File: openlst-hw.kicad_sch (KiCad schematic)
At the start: 54 parts, among them J1 CC Prog/Debug, J2 UART0, J7 Control Outputs, U1 CC1110, U2 MIC803, X1 TG2520SMN 27MHz

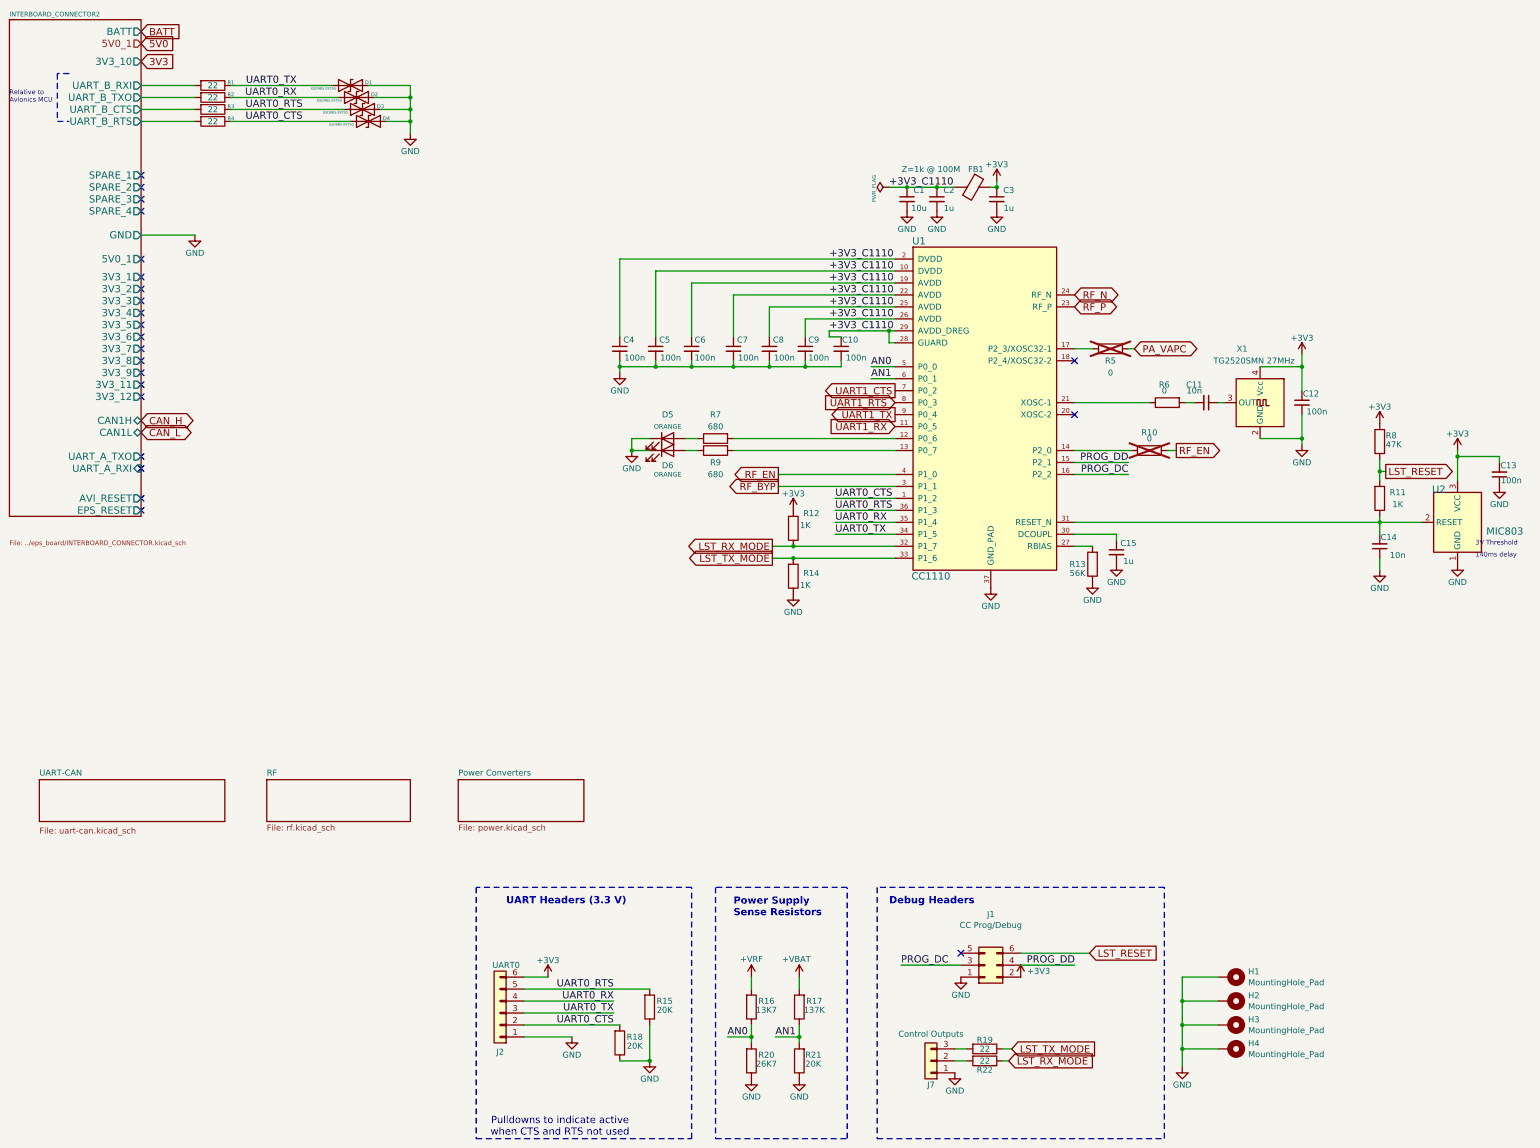
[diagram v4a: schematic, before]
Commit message: further refactor schema into subsheets
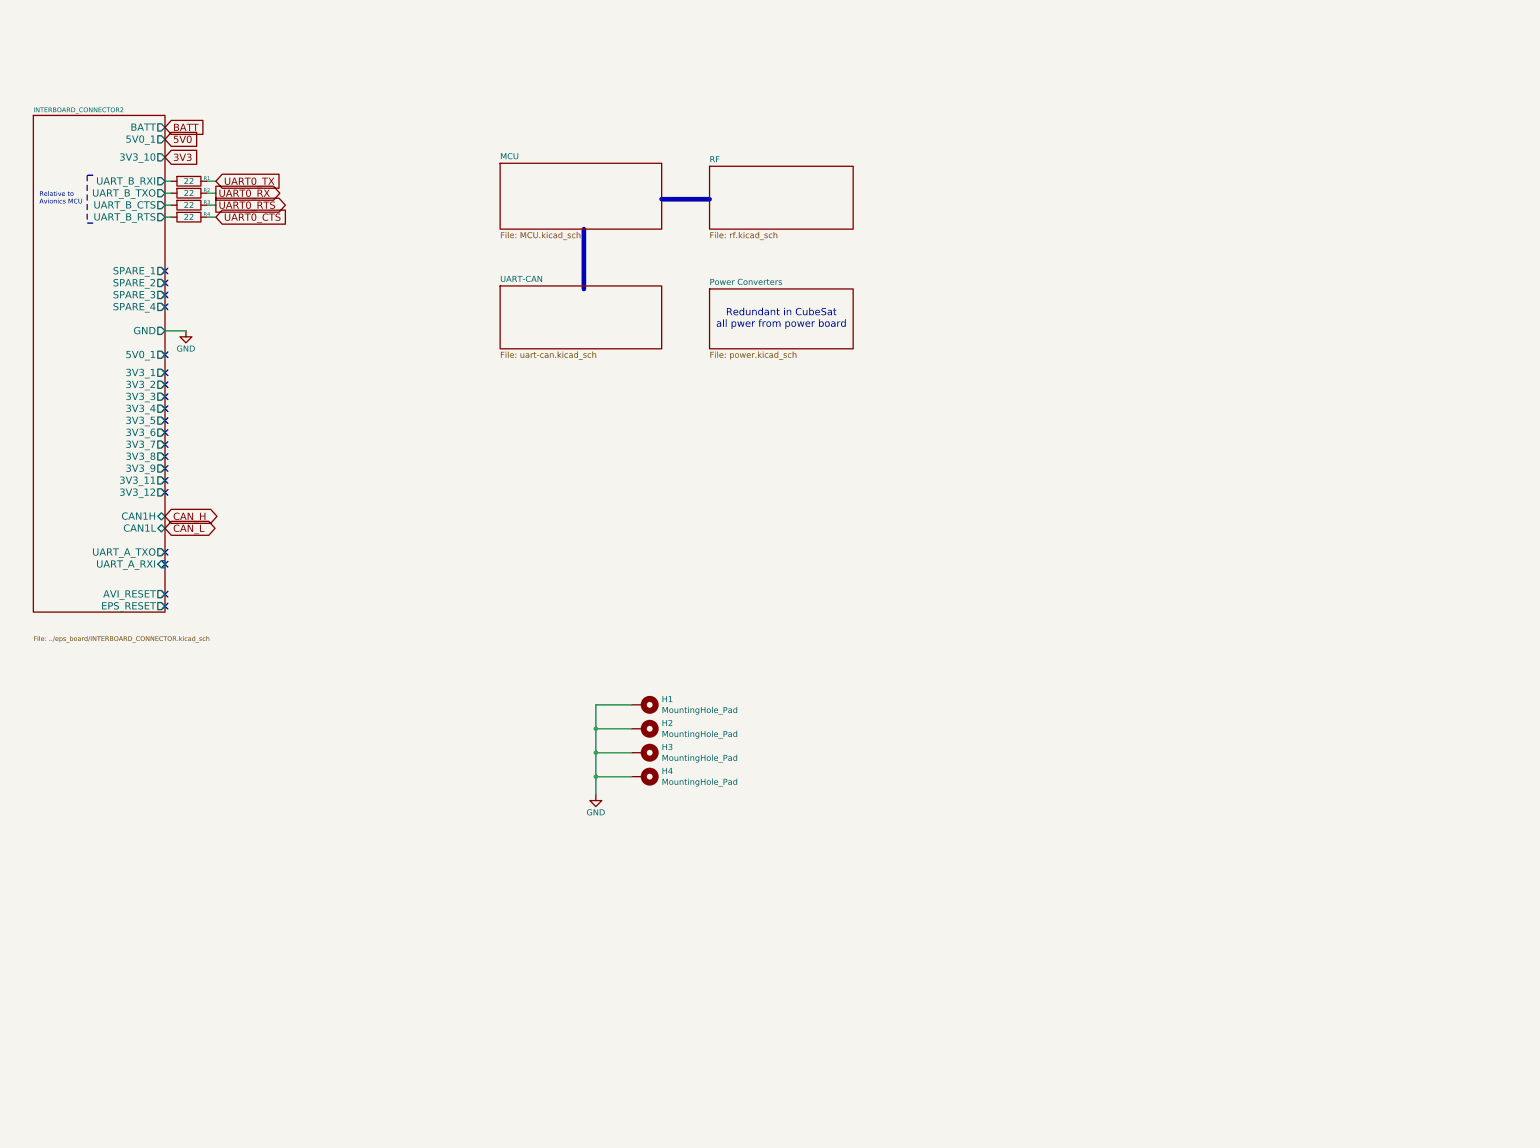
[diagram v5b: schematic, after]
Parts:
- removed C1: 10u, Capacitor_SMD:C_0603_1608Metric_Pad1.08x0.95mm_HandSolder, symbol Device:C_Small
- removed C10, C12, C13, C4, C5, C6, C7, C8, C9: 100n, Capacitor_SMD:C_0402_1005Metric_Pad0.74x0.62mm_HandSolder, symbol Device:C_Small
- removed C11, C14: 10n, Capacitor_SMD:C_0603_1608Metric_Pad1.08x0.95mm_HandSolder, symbol Device:C_Small
- removed C15, C2, C3: 1u, Capacitor_SMD:C_0603_1608Metric_Pad1.08x0.95mm_HandSolder, symbol Device:C_Small
- removed D1, D2, D3, D4: ESD9B5.0ST5G, LED_SMD:LED_0603_1608Metric_Pad1.05x0.95mm_HandSolder, symbol Diode:ESD9B5.0ST5G
- removed D5, D6: ORANGE, LED_SMD:LED_0603_1608Metric_Pad1.05x0.95mm_HandSolder, symbol Device:LED
- removed FB1: Z=1k @ 100M, Inductor_SMD:L_0603_1608Metric_Pad1.05x0.95mm_HandSolder, symbol Device:FerriteBead
- removed J1: CC Prog/Debug, Connector_PinHeader_2.54mm:PinHeader_2x03_P2.54mm_Vertical, symbol Connector_Generic:Conn_02x03_Odd_Even
- removed J2: UART0, Connector_PinHeader_2.54mm:PinHeader_1x06_P2.54mm_Vertical, symbol Connector_Generic:Conn_01x06
- removed J7: Control Outputs, Connector_PinHeader_2.54mm:PinHeader_1x03_P2.54mm_Vertical, symbol Connector_Generic:Conn_01x03
- removed R10, R5, R6: 0, Resistor_SMD:R_0603_1608Metric_Pad0.98x0.95mm_HandSolder, symbol Device:R
- removed R11, R12, R14: 1K, Resistor_SMD:R_0603_1608Metric_Pad0.98x0.95mm_HandSolder, symbol Device:R
- removed R13: 56K, Resistor_SMD:R_0603_1608Metric_Pad0.98x0.95mm_HandSolder, symbol Device:R
- removed R15, R18, R21: 20K, Resistor_SMD:R_0603_1608Metric_Pad0.98x0.95mm_HandSolder, symbol Device:R
- removed R16: 13K7, Resistor_SMD:R_0603_1608Metric_Pad0.98x0.95mm_HandSolder, symbol Device:R
- removed R17: 137K, Resistor_SMD:R_0603_1608Metric_Pad0.98x0.95mm_HandSolder, symbol Device:R
- removed R19, R22: 22, Resistor_SMD:R_0603_1608Metric_Pad0.98x0.95mm_HandSolder, symbol Device:R
- removed R20: 26K7, Resistor_SMD:R_0603_1608Metric_Pad0.98x0.95mm_HandSolder, symbol Device:R
- removed R7, R9: 680, Resistor_SMD:R_0603_1608Metric_Pad0.98x0.95mm_HandSolder, symbol Device:R
- removed R8: 47K, Resistor_SMD:R_0603_1608Metric_Pad0.98x0.95mm_HandSolder, symbol Device:R
- removed U1: CC1110, Project:Texas_RHH0036C_VQFN-36-1EP_6x6mm_P0.5mm_EP4.4x4.4mm_ThermalVias, symbol Project:CC1110
- removed U2: MIC803, Package_TO_SOT_SMD:SOT-23_Handsoldering, symbol Project:MIC803
- removed X1: TG2520SMN 27MHz, Project:Oscillator_SMD_SeikoEpson_TG2520SMN-xxx-xxxxxx-4Pin_2.5x2.0mm, symbol Oscillator:TG2520SMN-xx.xxxxxxMhz-xxxxNM
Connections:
- no-connect marks 23 -> 20
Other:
- added sheet MCU (MCU.kicad_sch)
- note added: "Redundant in CubeSat all pwer from power board"
- note removed: "140ms delay"
- note removed: "3V Threshold"
- note removed: "Debug Headers"
- note removed: "Power Supply Sense Resistors"
- note removed: "Pulldowns to indicate active when CTS and RTS not used"
- note removed: "UART Headers (3.3 V)"
- moved on the sheet: H1, H2, H3, H4, R1, R2, R3, R4

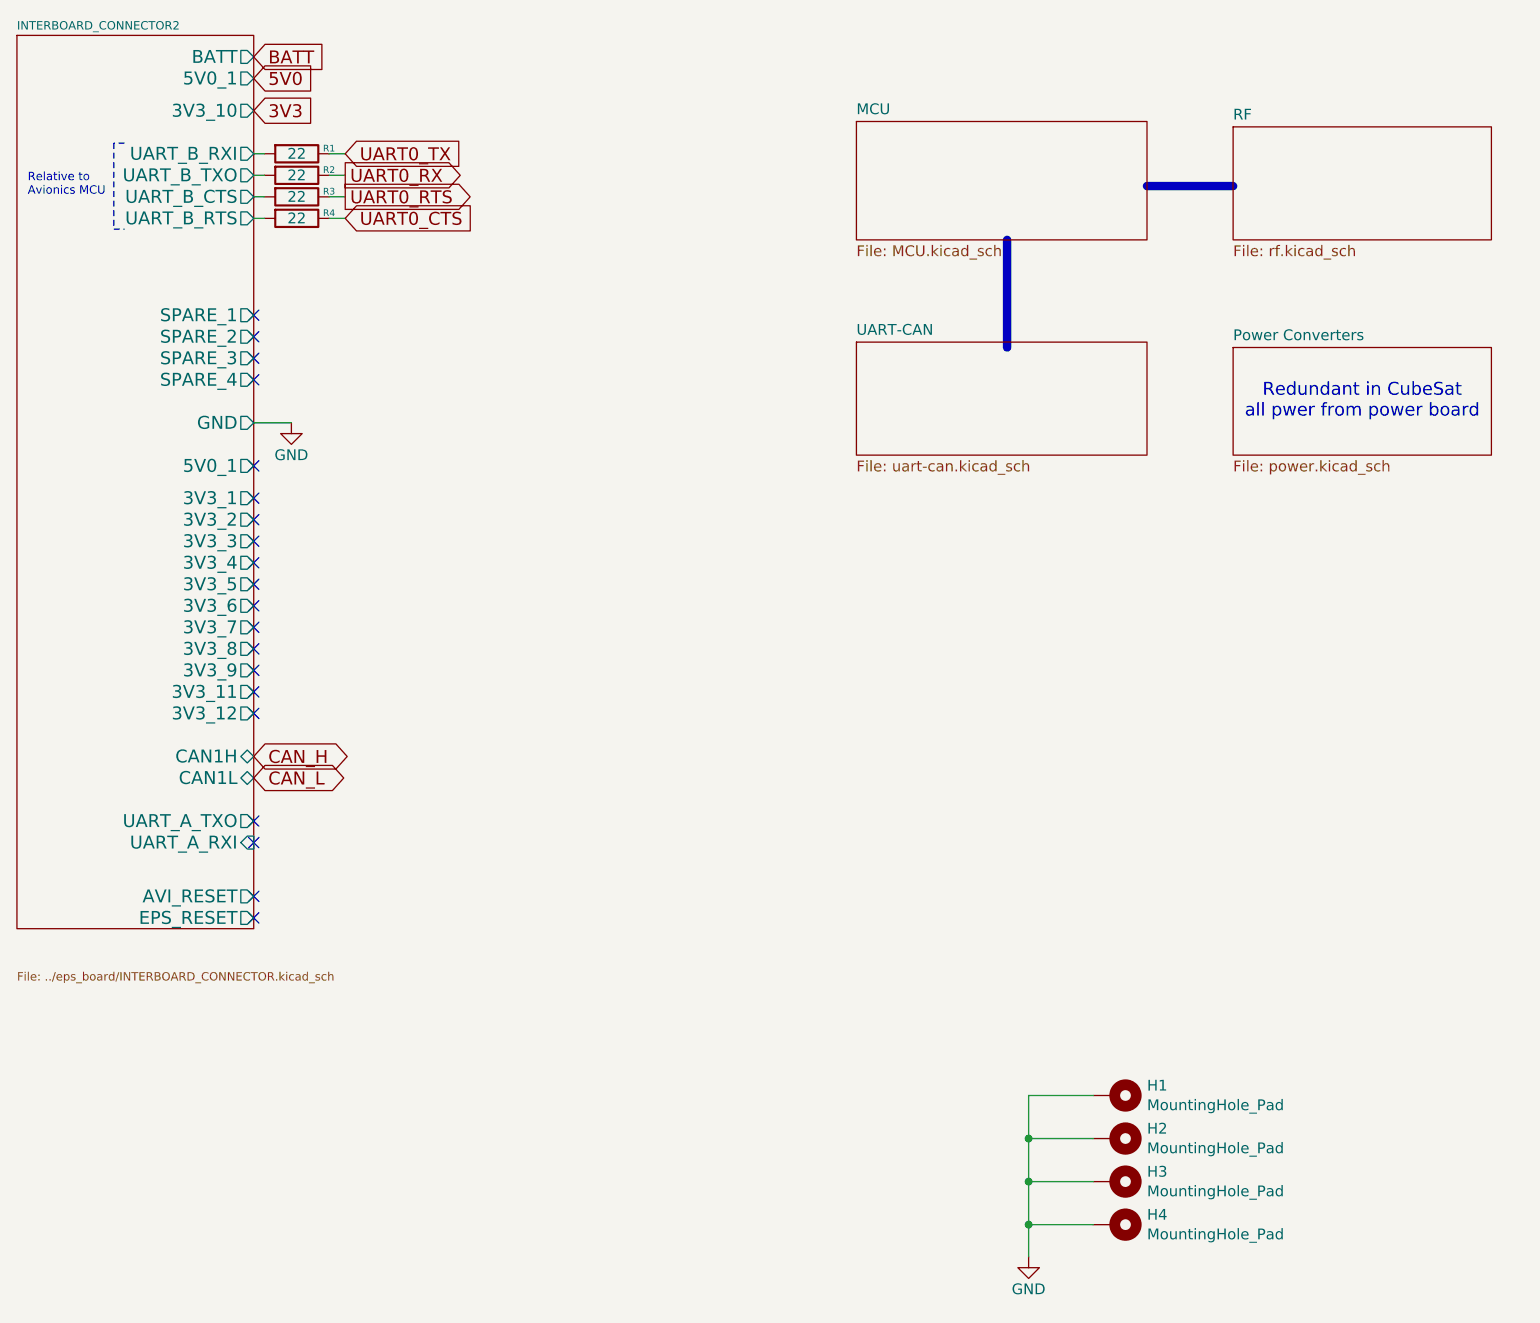
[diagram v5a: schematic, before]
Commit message: automatic schematic and pcb valiadation and cleanup
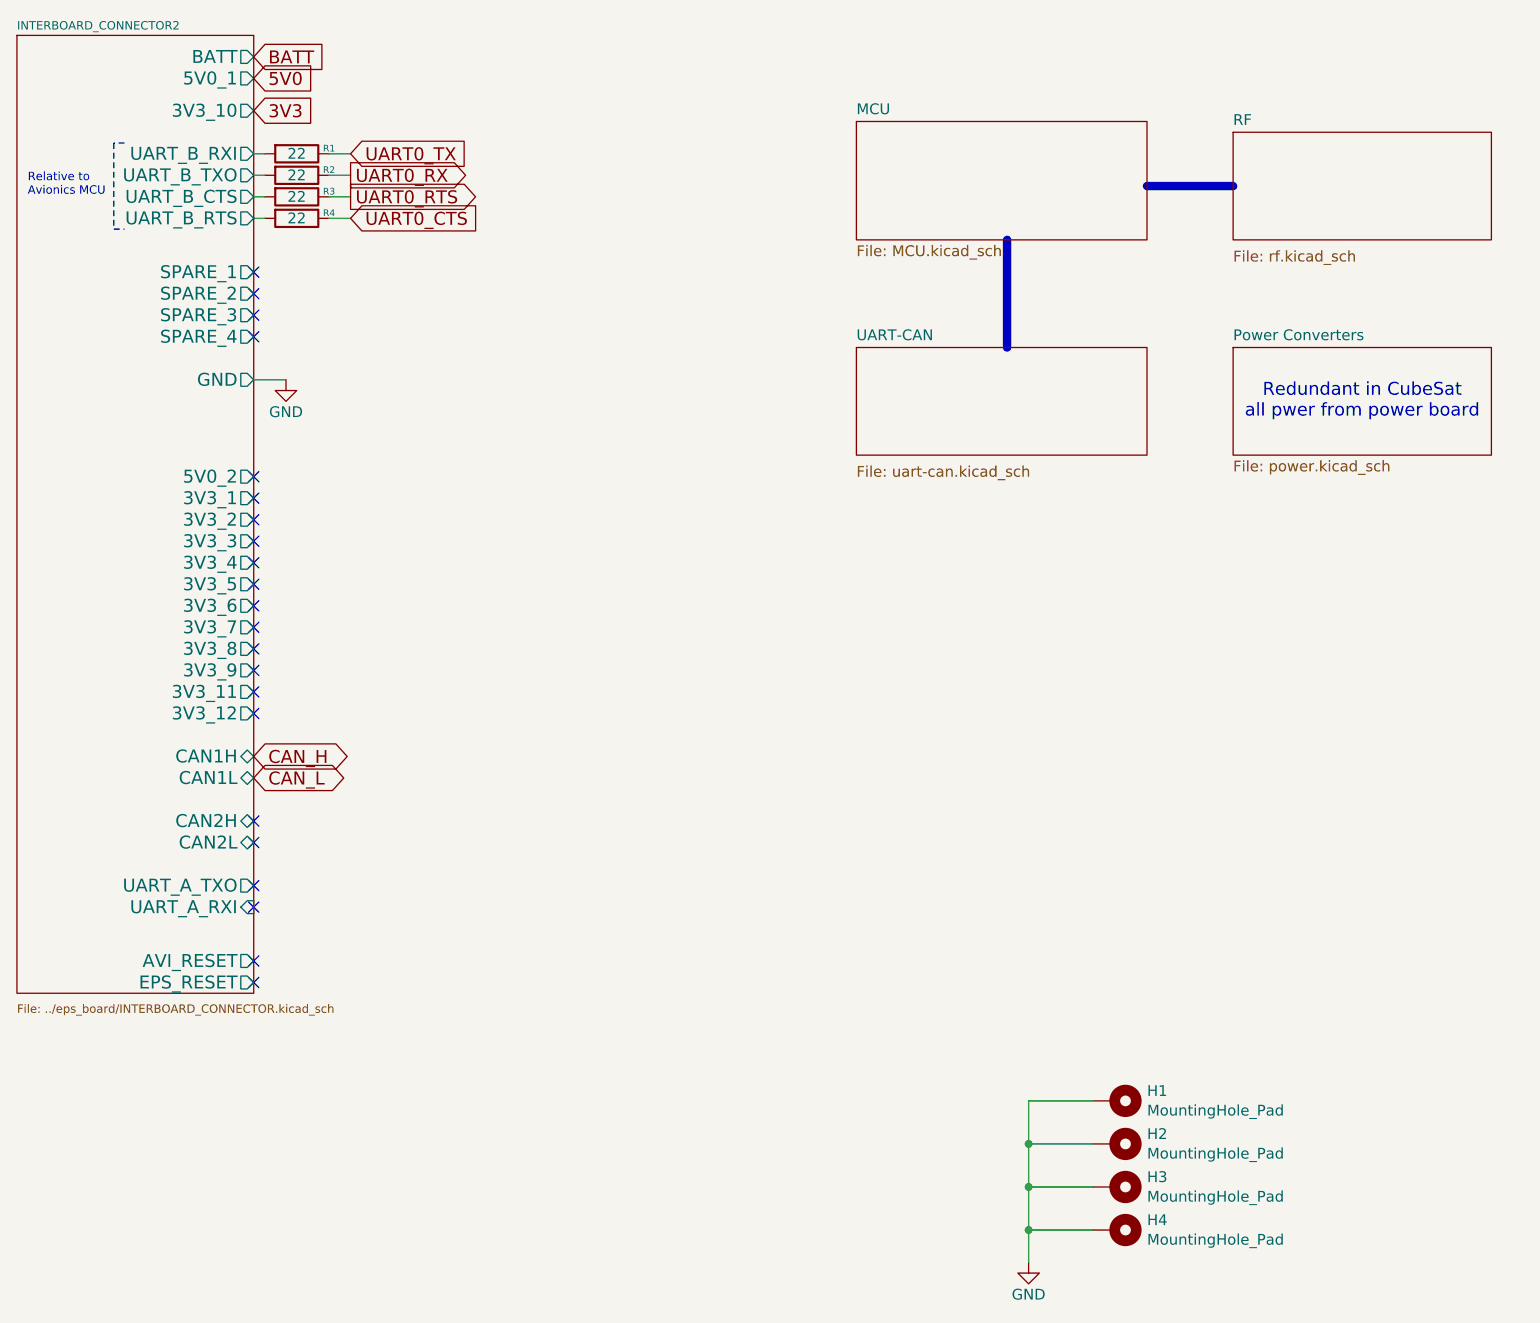
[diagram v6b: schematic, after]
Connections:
- no-connect marks 20 -> 22
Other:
- sheet INTERBOARD_CONNECTOR2 ports: added 5V0_2, CAN2H, CAN2L; removed none
- moved on the sheet: H1, H2, H3, H4

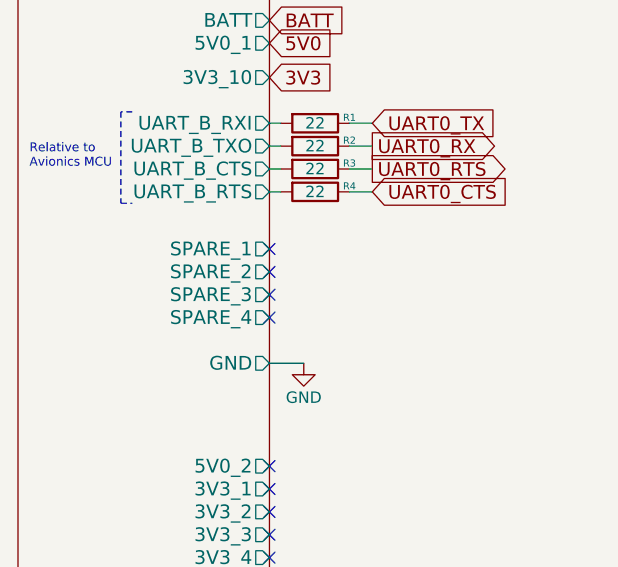
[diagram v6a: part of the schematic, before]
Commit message: cleanup openlst board after connector update
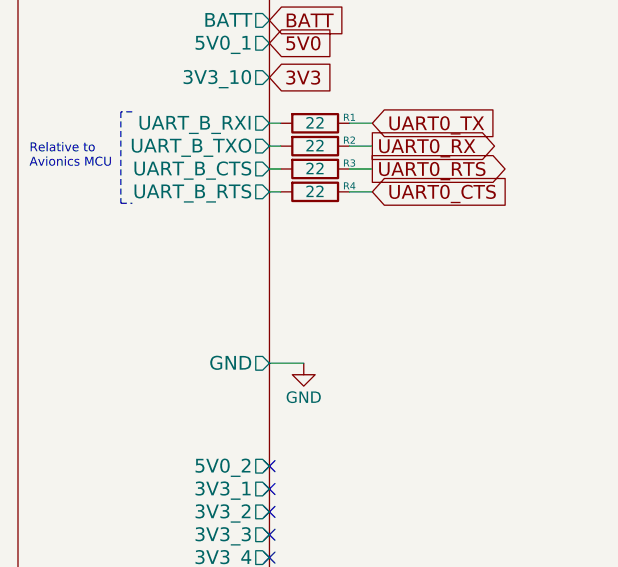
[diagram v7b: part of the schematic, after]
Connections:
- no-connect marks 22 -> 18
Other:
- sheet INTERBOARD_CONNECTOR2 ports: added none; removed SPARE_1, SPARE_2, SPARE_3, SPARE_4
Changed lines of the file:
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@@
-	)
-	(no_connect
-		(at 49.53 76.2)
 	)
 	(no_connect
@@
 	)
 	(no_connect
-		(at 49.53 73.66)
-	)
-	(no_connect
 		(at 49.53 148.59)
 	)
@@
 	)
 	(no_connect
-		(at 49.53 78.74)
-	)
-	(no_connect
 		(at 49.53 97.79)
 	)
@@
 	(no_connect
 		(at 49.53 113.03)
-	)
-	(no_connect
-		(at 49.53 81.28)
 	)
 	(no_connect
@@
 			)
 		)
-		(pin "SPARE_1" output
-			(at 49.53 73.66 0)
-			(effects
-				(font
-					(size 1.524 1.524)
-				)
-				(justify right)
-			)
-		)
-		(pin "SPARE_2" output
-			(at 49.53 76.2 0)
-			(effects
-				(font
-					(size 1.524 1.524)
-				)
-				(justify right)
-			)
-		)
-		(pin "SPARE_3" output
-			(at 49.53 78.74 0)
-			(effects
-				(font
-					(size 1.524 1.524)
-				)
-				(justify right)
-			)
-		)
 		(pin "UART_B_RXI" output
 			(at 49.53 59.69 0)
@@
 			(effects
 				(font
-					(size 1.524 1.524)
-				)
-				(justify right)
-			)
-		)
-		(pin "SPARE_4" output
-			(at 49.53 81.28 0)
-			(effects
-				(font
